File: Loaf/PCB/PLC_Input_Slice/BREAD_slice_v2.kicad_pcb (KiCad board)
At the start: 2 copper layers, 100 x 70.6 mm, 8 parts, among them J1 10018783-10200TLF, U2 MCP3208

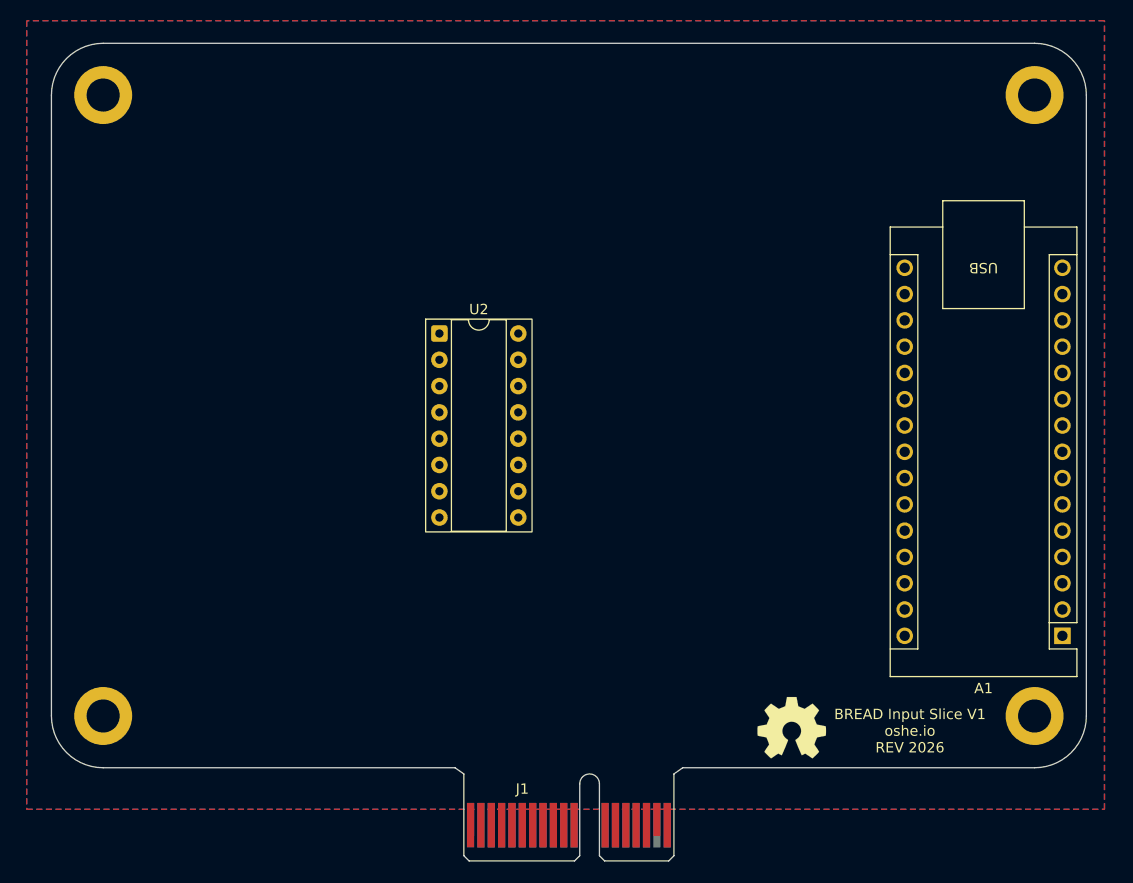
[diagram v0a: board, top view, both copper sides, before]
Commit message: Updated IO slice schematic
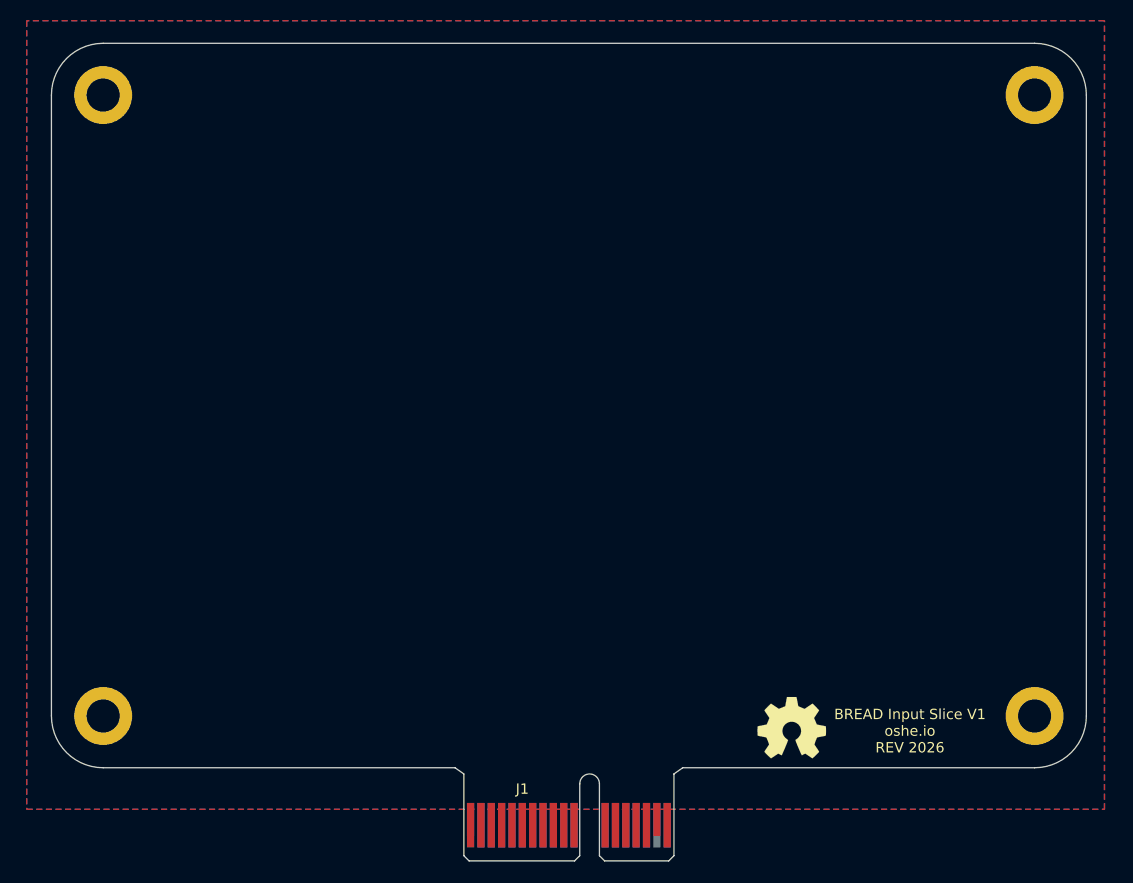
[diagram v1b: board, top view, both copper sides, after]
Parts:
- removed A1: Arduino_Nano_Every, Module:Arduino_Nano
- removed U2: MCP3208, Package_DIP:DIP-16_W7.62mm_Socket

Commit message: Preliminary PCB Design
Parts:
- added A1: Arduino_Nano_Every, Module:Arduino_Nano, F.Cu at (123.2, 115.6)
- added C1: 20pf, Capacitor_SMD:C_1206_3216Metric_Pad1.33x1.80mm_HandSolder, F.Cu at (197.6, 84.8)
- added C2: 20pf, Capacitor_SMD:C_1206_3216Metric_Pad1.33x1.80mm_HandSolder, F.Cu at (197.6, 68.8)
- added J3: DB25_Socket, Connector_Dsub:DSUB-25_Socket_Horizontal_P2.77x2.84mm_EdgePinOffset4.94mm_Housed_MountingHolesOffset4.94mm, F.Cu at (109.8, 107.1)
- added R1: 10k, Resistor_SMD:R_1206_3216Metric_Pad1.30x1.75mm_HandSolder, F.Cu at (182.5, 91.8)
- added R2: 10k, Resistor_SMD:R_1206_3216Metric_Pad1.30x1.75mm_HandSolder, F.Cu at (181.1, 98.4)
- added R3: 10k, Resistor_THT:R_Axial_DIN0207_L6.3mm_D2.5mm_P10.16mm_Horizontal, F.Cu at (182.4, 64.0)
- added R4: 10k, Resistor_THT:R_Axial_DIN0207_L6.3mm_D2.5mm_P10.16mm_Horizontal, F.Cu at (177.5, 57.7)
- added R5: 10k, Resistor_THT:R_Axial_DIN0207_L6.3mm_D2.5mm_P10.16mm_Horizontal, F.Cu at (161.5, 96.0)
- added R6: 10k, Resistor_THT:R_Axial_DIN0207_L6.3mm_D2.5mm_P10.16mm_Horizontal, F.Cu at (165.1, 96.8)
- added RN1: 10K Resistor Array, Resistor_THT:R_Array_SIP9, F.Cu at (115.0, 92.5)
- added RN2: 10K Resistor Array, Resistor_THT:R_Array_SIP9, F.Cu at (115.0, 65.5)
- added U1: MCP4922-EP, Package_DIP:DIP-14_W10.16mm_LongPads, F.Cu at (138.7, 57.9)
- added U2: MCP4922-EP, Package_DIP:DIP-14_W10.16mm_LongPads, F.Cu at (157.7, 57.9)
- added U3: MCP4922-EP, Package_DIP:DIP-14_W10.16mm_LongPads, F.Cu at (142.5, 94.7)
- added U4: MCP4922-EP, Package_DIP:DIP-14_W10.16mm_LongPads, F.Cu at (123.4, 94.7)
- added U5: MCP3208, Package_DIP:DIP-16_W7.62mm_LongPads, F.Cu at (166.6, 67.4)
- added U6: MCP2561-E-P, Package_DIP:DIP-8_W7.62mm, F.Cu at (193.0, 106.0)
- added U7: MCP2515-xSO, Package_DIP:DIP-18_W7.62mm, F.Cu at (193.0, 93.3)
- added Y1: 16MHZ Crystal, Crystal:Crystal_HC49-4H_Vertical, F.Cu at (197.6, 74.4)
- moved Logo1 59.3 mm to (113.7, 121.3)
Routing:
- net /MOSI: track 0.00 -> 180.5 mm, vias 0 -> 4
- net /SCK: track 0.00 -> 167.0 mm, vias 0 -> 4
- net /DAC1: track 0.00 -> 124.0 mm, vias 0 -> 2
- net /DAC2: track 0.00 -> 110.0 mm, vias 0 -> 2
- net /SHDN: track 0.00 -> 109.0 mm, vias 0 -> 2
- net /INT: track 0.00 -> 78.8 mm
- net /AIO3: track 0.00 -> 71.6 mm
- net /AIO1: track 0.00 -> 71.0 mm, vias 0 -> 1
- net /AIO5: track 0.00 -> 70.4 mm, vias 0 -> 1
- net /AIO0: track 0.00 -> 70.3 mm, vias 0 -> 1
- net /AIO7: track 0.00 -> 68.9 mm, vias 0 -> 1
- net /AIO4: track 0.00 -> 68.8 mm
- net /AIO2: track 0.00 -> 68.5 mm, vias 0 -> 1
- net /ESTOP: track 0.00 -> 68.4 mm, vias 0 -> 2
- net /AIO6: track 0.00 -> 67.4 mm, vias 0 -> 1
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- added copper zone on F.Cu, net +3.3V

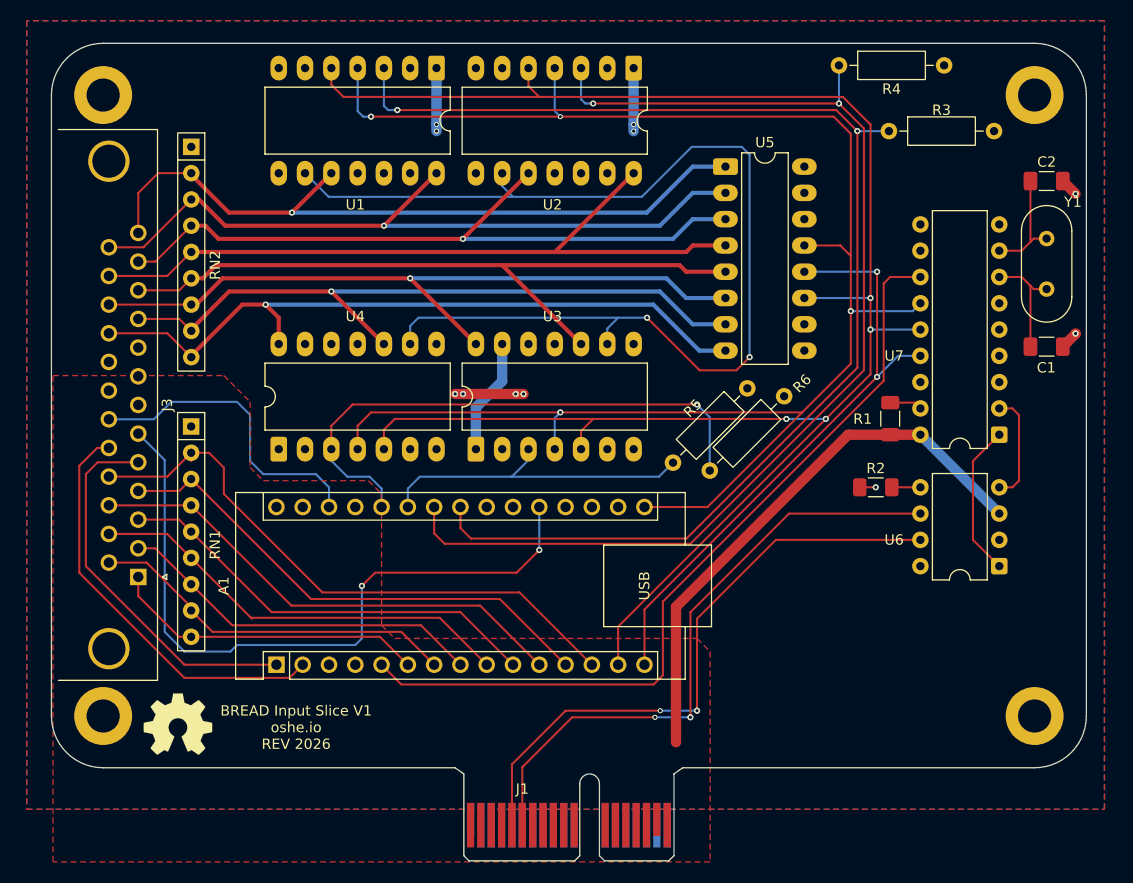
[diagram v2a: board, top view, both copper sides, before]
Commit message: Added optional VRM and switched to 5V ADC and DAC
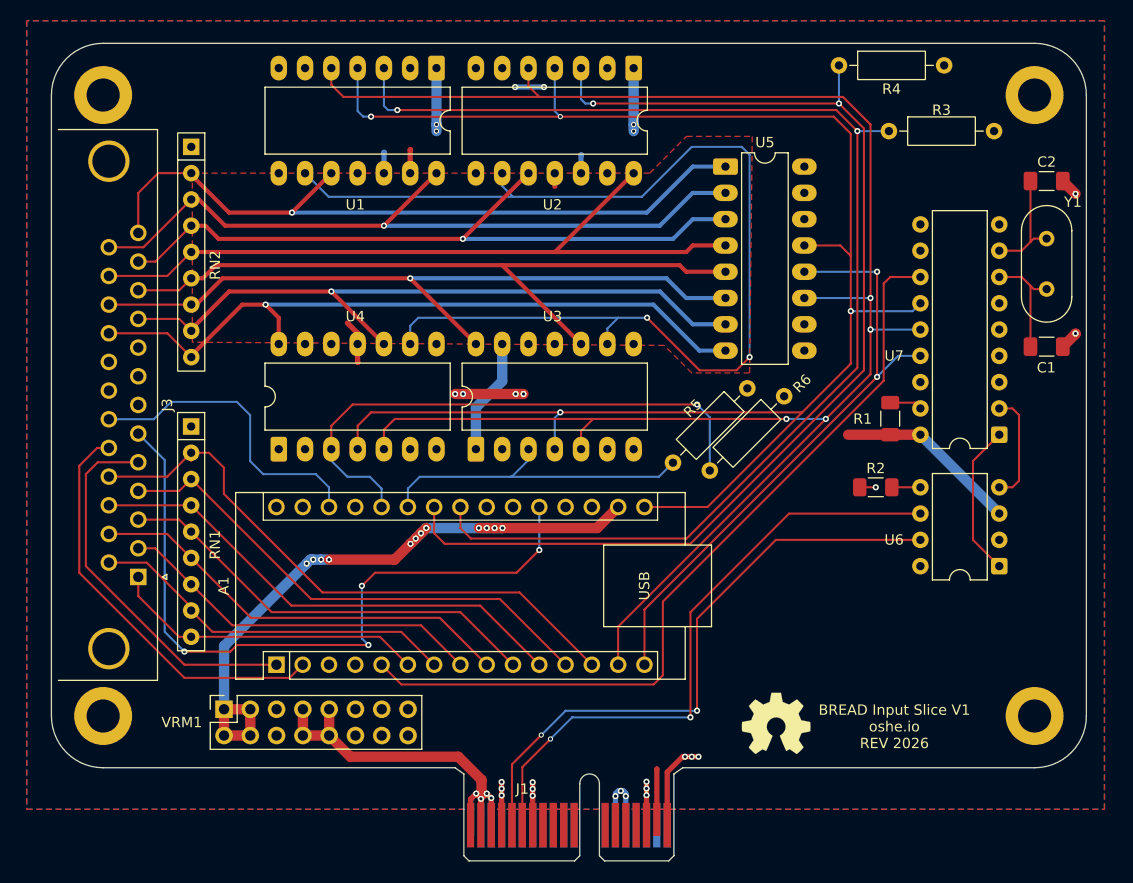
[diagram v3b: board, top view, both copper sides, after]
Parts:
- added VRM1: Optional VRM, Connector_PinSocket_2.54mm:PinSocket_2x08_P2.54mm_Vertical, F.Cu at (118.1, 119.9)
- moved Logo1 57.8 mm to (171.5, 121.2)
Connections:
- U1 pad 1: +3.3V -> +5V
- U1 pad 11: +3.3V -> +5V
- U1 pad 13: +3.3V -> +5V
- U2 pad 1: +3.3V -> +5V
- U2 pad 11: +3.3V -> +5V
- U2 pad 13: +3.3V -> +5V
- U3 pad 1: +3.3V -> +5V
- U3 pad 11: +3.3V -> +5V
- U3 pad 13: +3.3V -> +5V
- U4 pad 1: +3.3V -> +5V
- U4 pad 11: +3.3V -> +5V
- U4 pad 13: +3.3V -> +5V
- U5 pad 15: +3.3V -> +5V
- U5 pad 16: +3.3V -> +5V
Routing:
- net +12V: track 0.00 -> 53.0 mm, vias 0 -> 4
- net +3.3V: track 23.4 -> 64.3 mm, vias 4 -> 12
- net GND: track 11.7 -> 36.8 mm, vias 7 -> 19
- net +5V: track 54.4 -> 64.0 mm, vias 0 -> 9
- net /ESTOP: track 68.4 -> 69.7 mm, vias 2 -> 4
- added copper zone on F.Cu, net GND
- removed copper zone on F.Cu, net +3.3V

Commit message: Saved PCB
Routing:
- net +3.3V: track 64.3 -> 66.7 mm
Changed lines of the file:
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@@
+	)
+	(segment
+		(start 128.27 105.41)
+		(end 126.492 105.41)
+		(width 1)
+		(layer "F.Cu")
+		(net "+3.3V")
 	)
 	(segment
@@
 		(width 1)
 		(layer "F.Cu")
+		(net "+3.3V")
+	)
+	(segment
+		(start 126.492 105.41)
+		(end 126.111 105.791)
+		(width 1)
+		(layer "F.Cu")

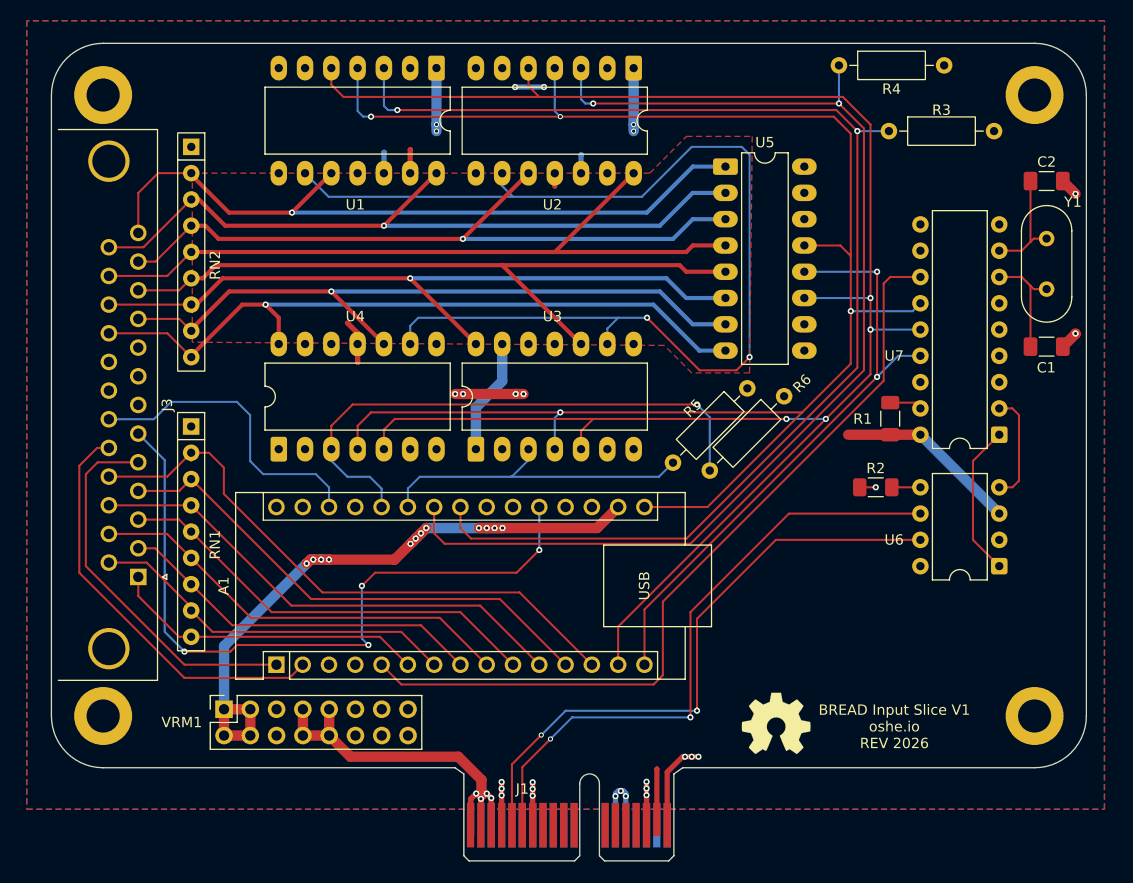
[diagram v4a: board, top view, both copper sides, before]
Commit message: Added power filter caps
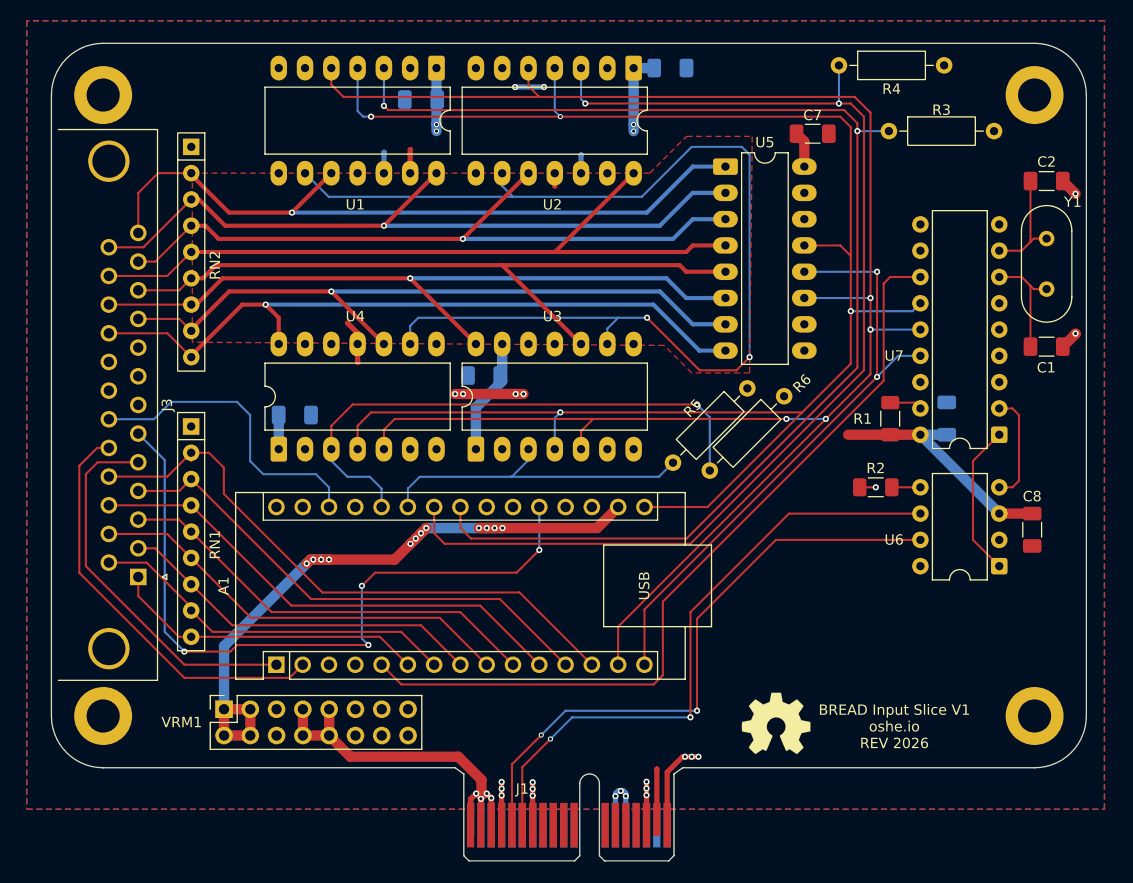
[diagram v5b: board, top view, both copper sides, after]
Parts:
- added C3: 0.47uF, Capacitor_SMD:C_1206_3216Metric_Pad1.33x1.80mm_HandSolder, B.Cu at (137.2, 61.0)
- added C4: 0.47uF, Capacitor_SMD:C_1206_3216Metric_Pad1.33x1.80mm_HandSolder, B.Cu at (161.3, 57.9)
- added C5: 0.47uF, Capacitor_SMD:C_1206_3216Metric_Pad1.33x1.80mm_HandSolder, B.Cu at (125.0, 91.4)
- added C6: 0.47uF, Capacitor_SMD:C_1206_3216Metric_Pad1.33x1.80mm_HandSolder, B.Cu at (143.3, 87.6)
- added C7: 0.47uF, Capacitor_SMD:C_1206_3216Metric_Pad1.33x1.80mm_HandSolder, F.Cu at (175.0, 64.3)
- added C8: 0.47uF, Capacitor_SMD:C_1206_3216Metric_Pad1.33x1.80mm_HandSolder, F.Cu at (196.2, 102.5)
- added C9: 0.47uF, Capacitor_SMD:C_1206_3216Metric_Pad1.33x1.80mm_HandSolder, B.Cu at (188.0, 91.8)
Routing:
- net +5V: track 64.0 -> 78.5 mm
- net /MOSI: track 180.5 -> 181.1 mm
- net /DAC2: track 110.0 -> 110.7 mm

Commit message: Add files via upload
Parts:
- removed C9: 0.47uF, Capacitor_SMD:C_1206_3216Metric_Pad1.33x1.80mm_HandSolder
- added J2: Barrel Jack, Connector_BarrelJack:BarrelJack_SwitchcraftConxall_RAPC10U_Horizontal, F.Cu at (175.0, 74.2)
- moved R4 81.6 mm to (108.0, 100.4), turned to -90 degrees
- moved R3 80.1 mm to (111.0, 100.4), turned to -90 degrees
- moved C3 64.7 mm to (195.5, 89.0), turned to 180 degrees
- moved C8 61.8 mm to (134.5, 99.1)
- moved U5 59.2 mm to (107.9, 75.0)
- moved C4 52.7 mm to (110.0, 70.0)
- moved C7 51.4 mm to (142.4, 104.0), turned to 90 degrees
- moved RN2 47.6 mm to (162.4, 69.0), turned to 180 degrees
- moved J3 44.6 mm to (120.9, 63.8), turned to 180 degrees
- moved U1 41.6 mm to (120.5, 95.3), turned to 0 degrees
- moved U2 41.0 mm to (120.3, 74.8), turned to 0 degrees
- moved A1 38.7 mm to (161.9, 115.5)
- moved U4 36.1 mm to (155.9, 110.5), turned to 180 degrees
- moved RN1 31.2 mm to (135.4, 69.0), turned to 180 degrees
- moved U6 21.9 mm to (198.8, 85.0), turned to -90 degrees
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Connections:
- A1 pad 19: /SHDNTRIG -> /SHDN
- J1 pad A16: /EstpCh1 -> /ESTOP
- VRM1 pad 15: +5V -> +3.3V
- VRM1 pad 16: +5V -> +3.3V
- VRM1 pad 3: +3.3V -> +5V
- VRM1 pad 4: +3.3V -> +5V
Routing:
- net +12V: track 53.0 -> 172.3 mm, vias 4 -> 5
- net /ESTOP: track 69.7 -> 178.1 mm, vias 4 -> 2
- net GND: track 36.8 -> 141.9 mm, vias 19 -> 17
- net +5V: track 78.5 -> 174.8 mm, vias 9 -> 16
- net /MISO: track 59.3 -> 154.2 mm, vias 2 -> 1
- net /DIO0: track 30.9 -> 100.7 mm, vias 0 -> 3
- net /DIO1: track 35.7 -> 101.4 mm, vias 0 -> 3
- net /DIO2: track 35.8 -> 97.2 mm, vias 0 -> 3
- net /DIO3: track 41.8 -> 100.2 mm, vias 0 -> 3
- net /DIO4: track 42.0 -> 100.3 mm, vias 0 -> 3
- net /AIO0: track 70.3 -> 126.8 mm, vias 1 -> 0
- net /DIO5: track 48.0 -> 102.3 mm, vias 0 -> 3
- net /INT: track 78.8 -> 24.5 mm
- net /DIO6: track 49.2 -> 99.6 mm, vias 0 -> 3
- net /AIO2: track 68.5 -> 117.9 mm, vias 1 -> 0
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- removed copper zone on F.Cu, net GND
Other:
- board text added: "BREAD I/O Slice V1 oshe.io REV 2026"
- board text removed: "BREAD Input Slice V1 oshe.io REV 2026"
